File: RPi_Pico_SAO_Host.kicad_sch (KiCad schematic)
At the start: 11 parts, among them J1 SAO Host Header, J2 SAO Host Header

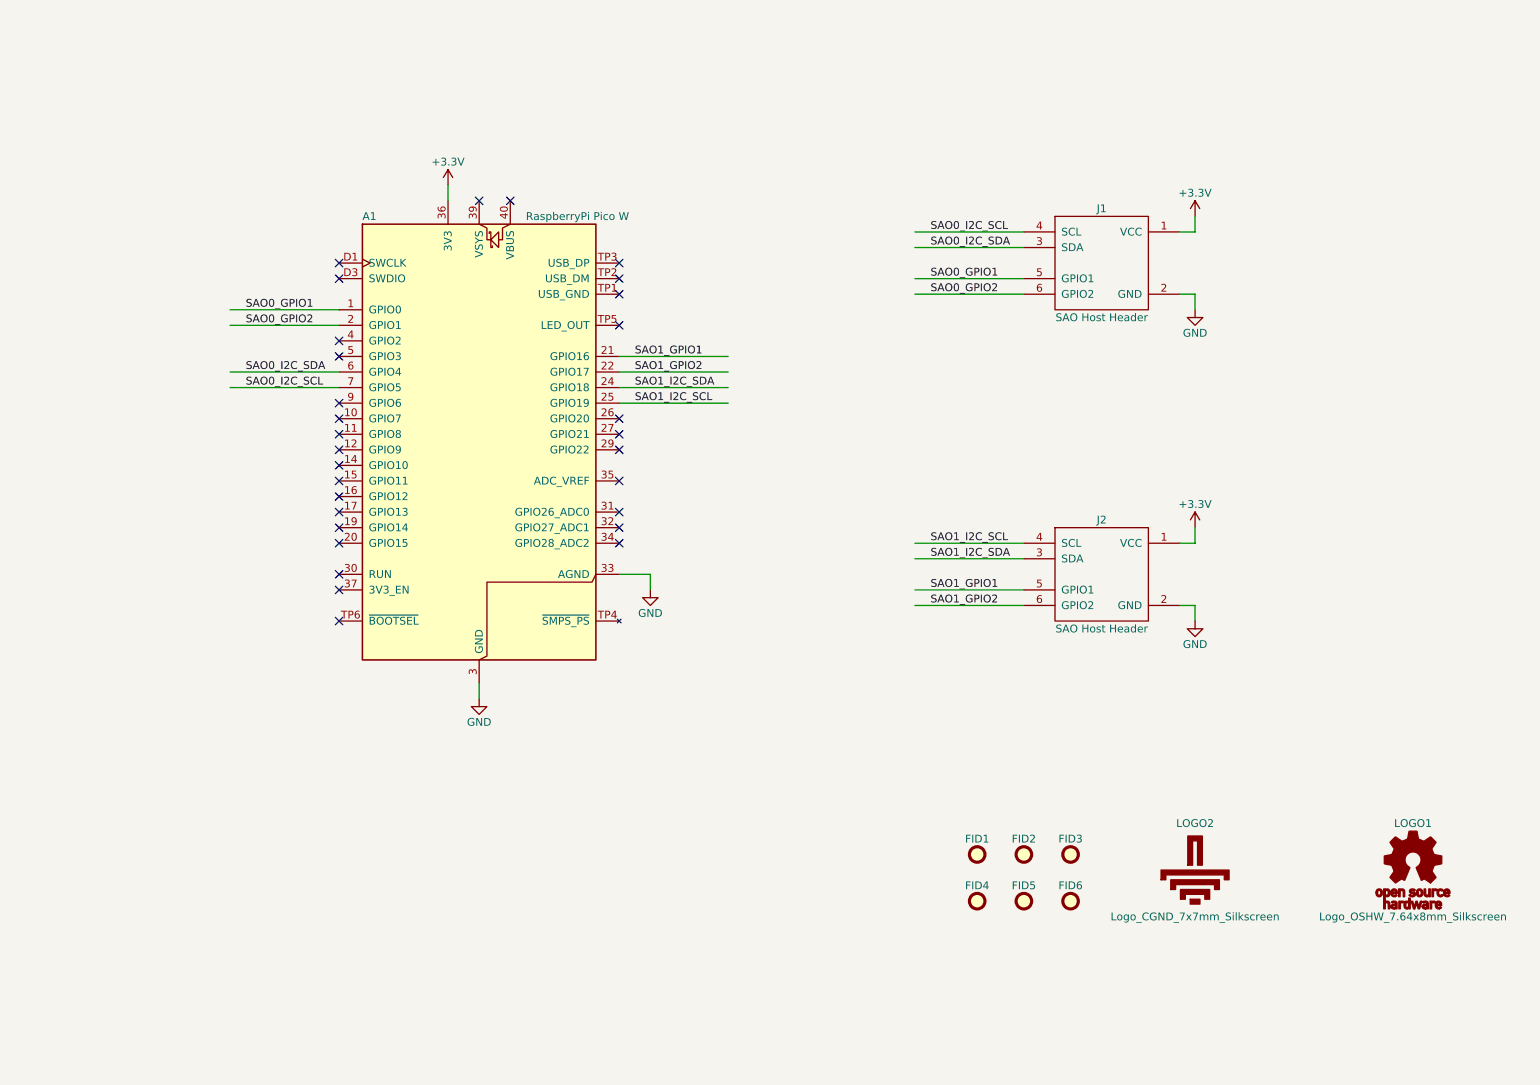
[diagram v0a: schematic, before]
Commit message: Add v2 design changes
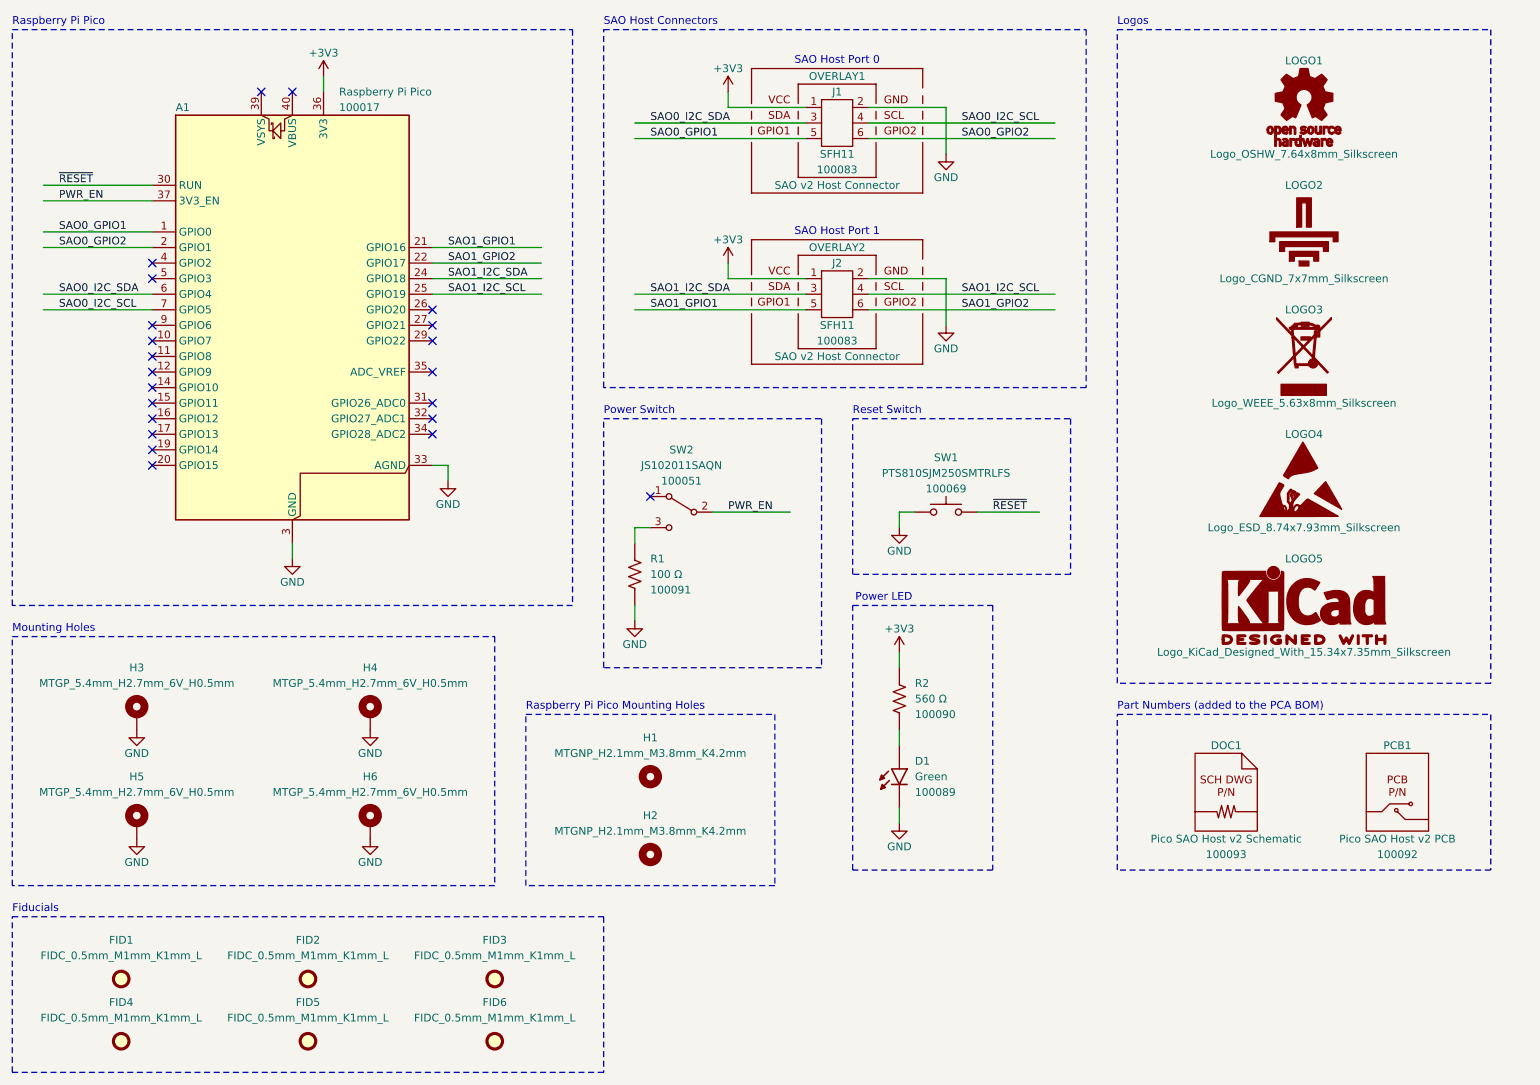
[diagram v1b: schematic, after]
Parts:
- removed A1: RaspberryPi Pico W, RPi_Pico_SAO_Host:RASPBERRY_PI_PICO_W, symbol RPi_Pico_SAO_Host:PCA_RaspberryPi_Pico_W
- removed FID1, FID2, FID3, FID4, FID5, FID6: Fiducial, RPi_Pico_SAO_Host:FIDC50M100K100L, symbol RPi_Pico_SAO_Host:Fiducial_c50m100k100
- removed J1, J2: SAO Host Header, RPi_Pico_SAO_Host:SULLINS_SFH11-NBPC-D03-ST-BK_SAO_V2, symbol RPi_Pico_SAO_Host:Connector_Header_2x03_P2.54mm_Vertical_SAO_Host_v2
- removed LOGO1: Logo_OSHW_7.64x8mm_Silkscreen, RPi_Pico_SAO_Host:LOGO_OSHW_764X800_SILKSCREEN, symbol RPi_Pico_SAO_Host:Logo_OSHW_7.64x8mm_Silkscreen
- removed LOGO2: Logo_CGND_7x7mm_Silkscreen, RPi_Pico_SAO_Host:LOGO_CGND_700X700_SILKSCREEN, symbol RPi_Pico_SAO_Host:Logo_CGND_7x7mm_Silkscreen
- added A1: Raspberry Pi Pico, CGND_Module:Raspberry_Pi_Pico_Common_SMD, symbol CGND_OSHW_IPN:100017
- added D1: Green, CGND_LED:LEDSC_0603_0.8x1.6x0.8mm_L0.45x0.7mm_N, symbol CGND_OSHW_IPN:100089
- added DOC1: Pico SAO Host v2 Schematic, symbol CGND_OSHW_IPN:100093
- added FID1, FID2, FID3, FID4, FID5, FID6: FIDC_0.5mm_M1mm_K1mm_L, CGND_Fiducial:FIDC_0.5mm_M1mm_K1mm_L, symbol CGND_Mechanical:FIDC_0.5mm_M1mm_K1mm_L
- added H1, H2: MTGNP_H2.1mm_M3.8mm_K4.2mm, CGND_Mounting_Hole:MTGNP_H2.1mm_M3.8mm_K4.2mm, symbol CGND_Mechanical:MTGNP_H2.1mm_M3.8mm_K4.2mm
- added H3, H4, H5, H6: MTGP_5.4mm_H2.7mm_6V_H0.5mm, CGND_Mounting_Hole:MTGP_5.4mm_H2.7mm_6V_H0.5mm, symbol CGND_Mechanical:MTGP_5.4mm_H2.7mm_6V_H0.5mm
- added J1, J2: SFH11, CGND_Connector:Sullins_SFH11-xxxC-D03-ST-BK, symbol CGND_OSHW_IPN:100083
- added LOGO1: Logo_OSHW_7.64x8mm_Silkscreen, CGND_Graphic:Logo_OSHW_7.64x8mm_Silkscreen, symbol CGND_Graphic:Logo_OSHW_7.64x8mm_Silkscreen
- added LOGO2: Logo_CGND_7x7mm_Silkscreen, CGND_Graphic:Logo_CGND_7x7mm_Silkscreen, symbol CGND_Graphic:Logo_CGND_7x7mm_Silkscreen
- added LOGO3: Logo_WEEE_5.63x8mm_Silkscreen, CGND_Graphic:Logo_WEEE_5.63x8mm_Silkscreen, symbol CGND_Graphic:Logo_WEEE_5.63x8mm_Silkscreen
- added LOGO4: Logo_ESD_8.74x7.93mm_Silkscreen, CGND_Graphic:Logo_ESD_8.74x7.93mm_Silkscreen, symbol CGND_Graphic:Logo_ESD_8.74x7.93mm_Silkscreen
- added LOGO5: Logo_KiCad_Designed_With_15.34x7.35mm_Silkscreen, CGND_Graphic:Logo_KiCad_Designed_With_15.34x7.35mm_Silkscreen, symbol CGND_Graphic:Logo_KiCad_Designed_With_15.34x7.35mm_Silkscreen
- added OVERLAY1, OVERLAY2: SAO v2 Host Connector, CGND_Connector:Overlay_SAO_v2_Host, symbol CGND_Connector:Connector_Overlay_SAO_v2_Host
- added PCB1: Pico SAO Host v2 PCB, symbol CGND_OSHW_IPN:100092
- added R1: 100 Ω, CGND_Resistor:RESC_0603_1.6x0.8x0.55mm_L0.25mm_N, symbol CGND_OSHW_IPN:100091
- added R2: 560 Ω, CGND_Resistor:RESC_0603_1.6x0.8x0.55mm_L0.25mm_N, symbol CGND_OSHW_IPN:100090
- added SW1: PTS810SJM250SMTRLFS, CGND_Switch:CK_PTS810SJx250, symbol CGND_OSHW_IPN:100069
- added SW2: JS102011SAQN, CGND_Switch:CK_JS102011SAxN, symbol CGND_OSHW_IPN:100051
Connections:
- net GND: now also A1.13 (GND), A1.18 (GND), A1.23 (GND), A1.28 (GND), A1.3 (GND), A1.33 (AGND), A1.38 (GND), A1.8 (GND), D1.C (Cathode), H3.1, H4.1, H5.1, H6.1, J1.2, J2.2, R1.2, SW1.1
- net SAO0_GPIO1: now also A1.1 (GPIO0), J1.5
- net SAO0_GPIO2: now also A1.2 (GPIO1), J1.6
- net SAO0_I2C_SCL: now also A1.7 (GPIO5), J1.4
- net SAO0_I2C_SDA: now also A1.6 (GPIO4), J1.3
- net SAO1_GPIO1: now also A1.21 (GPIO16), J2.5
- net SAO1_GPIO2: now also A1.22 (GPIO17), J2.6
- net SAO1_I2C_SCL: now also A1.25 (GPIO19), J2.4
- net SAO1_I2C_SDA: now also A1.24 (GPIO18), J2.3
- new net: R1.1, SW2.3 (C)
- new net: D1.A (Anode), R2.2
- new net +3V3: A1.36 (3V3), J1.1, J2.1, R2.1
- new net PWR_EN: A1.37 (3V3_EN), SW2.2 (B)
- new net ~{RESET}: A1.30 (RUN), SW1.2
- no-connect marks 30 -> 22
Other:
- note added: "Fiducials"
- note added: "Logos"
- note added: "Mounting Holes"
- note added: "Part Numbers (added to the PCA BOM)"
- note added: "Power LED"
- note added: "Power Switch"
- note added: "Raspberry Pi Pico"
- note added: "Raspberry Pi Pico Mounting Holes"
- note added: "Reset Switch"
- note added: "SAO Host Connectors"
- note added: "SAO Host Port 0"
- note added: "SAO Host Port 1"
- company: Common Ground Electronics -> ${ORGANIZATION} <${ORGANIZATION_URL}>
- title: Raspberry Pi Pico SAO Host v1 -> ${PROJECT_DESCRIPTION} v${PROJECT_VERSION_MAJOR}

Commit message: Remove old copyright & license fields
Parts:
- LOGO1, LOGO5: Symbol Copyright Common Ground Electronics <https://cgnd.dev>;The KiCad Deve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 -> (none); Symbol License CC-BY-SA-4.0 WITH KiCad-libraries-exception -> (none)
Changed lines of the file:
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@@
-			)
-		)
-		(property "Symbol Copyright" "Common Ground Electronics <https://cgnd.dev>;The KiCad Developers <https://www.kicad.org>"
-			(at 228.6 50.8 0)
-			(show_name yes)
-			(effects
-				(font
-					(size 1.27 1.27)
-				)
-				(hide yes)
-			)
-		)
-		(property "Symbol License" "CC-BY-SA-4.0 WITH KiCad-libraries-exception"
-			(at 228.6 53.34 0)
-			(show_name yes)
-			(effects
-				(font
-					(size 1.27 1.27)
-				)
-				(hide yes)
 			)
 		)
@@
 			(effects
 				(font
-					(size 1.27 1.27)
-				)
-				(hide yes)
-			)
-		)
-		(property "Symbol Copyright" "Common Ground Electronics <https://cgnd.dev>;The KiCad Developers <https://www.kicad.org>"
-			(at 228.6 129.54 0)
-			(show_name yes)
-			(effects
-				(font
-					(size 1.27 1.27)
-				)
-				(hide yes)
-			)
-		)
-		(property "Symbol License" "CC-BY-SA-4.0 WITH KiCad-libraries-exception"
-			(at 228.6 132.08 0)
-			(show_name yes)
-			(effects
-				(font

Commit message: Remove Symbol field from symbols and footprints
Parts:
- A1: Symbol CGND_TEMPLATE_Module:Raspberry_Pi_Pico -> (none)
- D1: Symbol CGND_TEMPLATE_Device:LED -> (none)
- DOC1: Symbol CGND_TEMPLATE_Part_Number:Schematic -> (none)
- J1, J2: Symbol CGND_TEMPLATE_Connector:Connector_2x3_Odd_Even -> (none)
- PCB1: Symbol CGND_TEMPLATE_Part_Number:PCB -> (none)
- R1, R2: Symbol CGND_TEMPLATE_Device:Resistor -> (none)
- SW1: Symbol CGND_TEMPLATE_Switch:Switch_Push_SPST-NO -> (none)
- SW2: Symbol CGND_TEMPLATE_Switch:Switch_SPDT -> (none)
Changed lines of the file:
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@@
 		)
 		(property "Footprint" "CGND_Resistor:RESC_0603_1.6x0.8x0.55mm_L0.25mm_N"
-			(at 109.22 109.22 0)
-			(show_name yes)
+			(at 111.76 109.22 0)
 			(effects
 				(font
@@
 				)
 				(justify left)
-			)
-		)
-		(property "Symbol" "CGND_TEMPLATE_Device:Resistor"
-			(at 111.76 109.22 0)
-			(show_name yes)
-			(effects
-				(font
-					(size 1.27 1.27)
-				)
-				(hide yes)
 			)
 		)
@@
 		)
 		(property "Footprint" "CGND_Resistor:RESC_0603_1.6x0.8x0.55mm_L0.25mm_N"
-			(at 152.4 129.54 0)
-			(show_name yes)
+			(at 154.94 129.54 0)
 			(effects
 				(font
@@
 			)
 		)
-		(property "Symbol" "CGND_TEMPLATE_Device:Resistor"
-			(at 154.94 129.54 0)
-			(show_name yes)
-			(effects
-				(font
-					(size 1.27 1.27)
-				)
-				(hide yes)
-			)
-		)
 		(pin "1"
 		)
@@
 		)
 		(property "Footprint" "CGND_Connector:Sullins_SFH11-xxxC-D03-ST-BK"
-			(at 152.4 53.34 0)
-			(show_name yes)
+			(at 152.4 50.8 0)
 			(effects
 				(font
@@
 					(size 1.27 1.27)
 				)
-			)
-		)
-		(property "Symbol" "CGND_TEMPLATE_Connector:Connector_2x3_Odd_Even"
-			(at 152.4 50.8 0)
-			(show_name yes)
-			(effects
-				(font
-					(size 1.27 1.27)
-				)
-				(hide yes)
 			)
 		)
@@
 		)
 		(property "Footprint" "CGND_LED:LEDSC_0603_0.8x1.6x0.8mm_L0.45x0.7mm_N"
-			(at 149.86 142.24 0)
-			(show_name yes)
+			(at 152.4 142.24 0)
 			(effects
 				(font
@@
 			)
 		)
-		(property "Symbol" "CGND_TEMPLATE_Device:LED"
-			(at 152.4 142.24 0)
-			(show_name yes)
-			(effects
-				(font
-					(size 1.27 1.27)
-				)
-				(hide yes)
-			)
-		)
 		(pin "A"
 		)
@@
 		)
 		(property "Footprint" "CGND_Switch:CK_PTS810SJx250"
-			(at 170.18 109.22 0)
-			(show_name yes)
+			(at 170.18 106.68 0)
 			(effects
 				(font
@@
 					(size 1.27 1.27)
 				)
-			)
-		)
-		(property "Symbol" "CGND_TEMPLATE_Switch:Switch_Push_SPST-NO"
-			(at 170.18 106.68 0)
-			(show_name yes)
-			(effects
-				(font
-					(size 1.27 1.27)
-				)
-				(hide yes)
 			)
 		)
@@
 			)
 		)
-		(property "Symbol" "CGND_TEMPLATE_Part_Number:Schematic"
-			(at 215.9 162.56 0)
-			(show_name yes)
-			(effects
-				(font
-					(size 1.27 1.27)
-				)
-				(hide yes)
-			)
-		)
 		(instances
 			(project ""
@@
 			)
 		)
-		(property "Symbol" "CGND_TEMPLATE_Part_Number:PCB"
-			(at 243.84 162.56 0)
-			(show_name yes)
-			(effects
-				(font
-					(size 1.27 1.27)
-				)
-				(hide yes)
-			)
-		)
 		(instances
 			(project ""
@@
 		)
 		(property "Footprint" "CGND_Connector:Sullins_SFH11-xxxC-D03-ST-BK"
-			(at 152.4 81.28 0)
-			(show_name yes)
+			(at 152.4 78.74 0)
 			(effects
 				(font
@@
 					(size 1.27 1.27)
 				)
-			)
-		)
-		(property "Symbol" "CGND_TEMPLATE_Connector:Connector_2x3_Odd_Even"
-			(at 152.4 78.74 0)
-			(show_name yes)
-			(effects
-				(font
-					(size 1.27 1.27)
-				)
-				(hide yes)
 			)
 		)
@@
 		)
 		(property "Footprint" "CGND_Switch:CK_JS102011SAxN"
-			(at 127 111.76 0)
-			(show_name yes)
+			(at 127 109.22 0)
 			(effects
 				(font
@@
 					(size 1.27 1.27)
 				)
-			)
-		)
-		(property "Symbol" "CGND_TEMPLATE_Switch:Switch_SPDT"
-			(at 127 109.22 0)
-			(show_name yes)
-			(effects
-				(font
-					(size 1.27 1.27)
-				)
-				(hide yes)
 			)
 		)
@@
 		)
 		(property "Footprint" "CGND_Module:Raspberry_Pi_Pico_Common_SMD"
-			(at 63.5 123.19 0)
-			(show_name yes)
+			(at 63.5 120.65 0)
 			(effects
 				(font
@@
 			)
 		)
-		(property "Symbol" "CGND_TEMPLATE_Module:Raspberry_Pi_Pico"
-			(at 63.5 120.65 0)
-			(show_name yes)
-			(effects
-				(font
-					(size 1.27 1.27)
-				)
-				(hide yes)
-			)
-		)
